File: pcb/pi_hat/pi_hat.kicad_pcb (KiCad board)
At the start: 2 copper layers, 65 x 56 mm, 3 parts, among them J1 Conn_02x20_Odd_Even, J2 RJ45, J3 RJ45

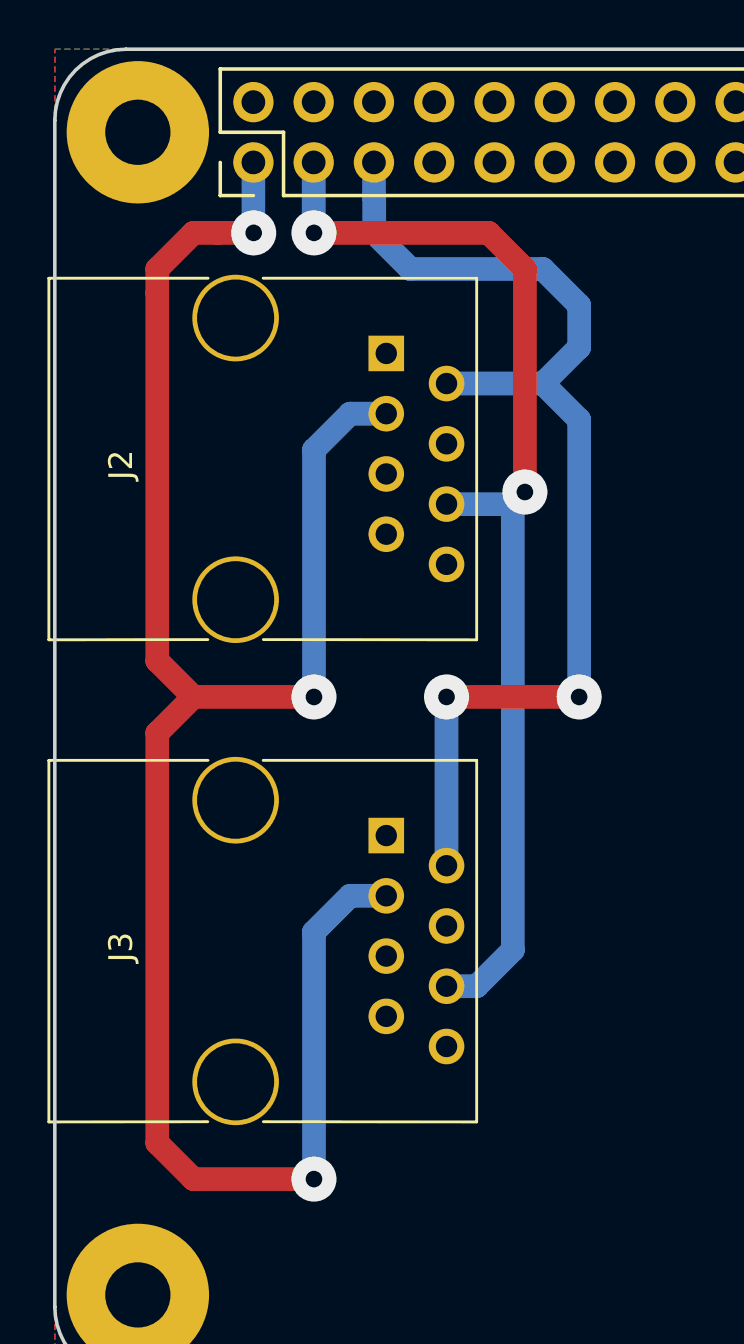
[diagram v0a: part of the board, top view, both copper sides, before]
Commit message: Trade the long ground loop for a 5th jumper :/
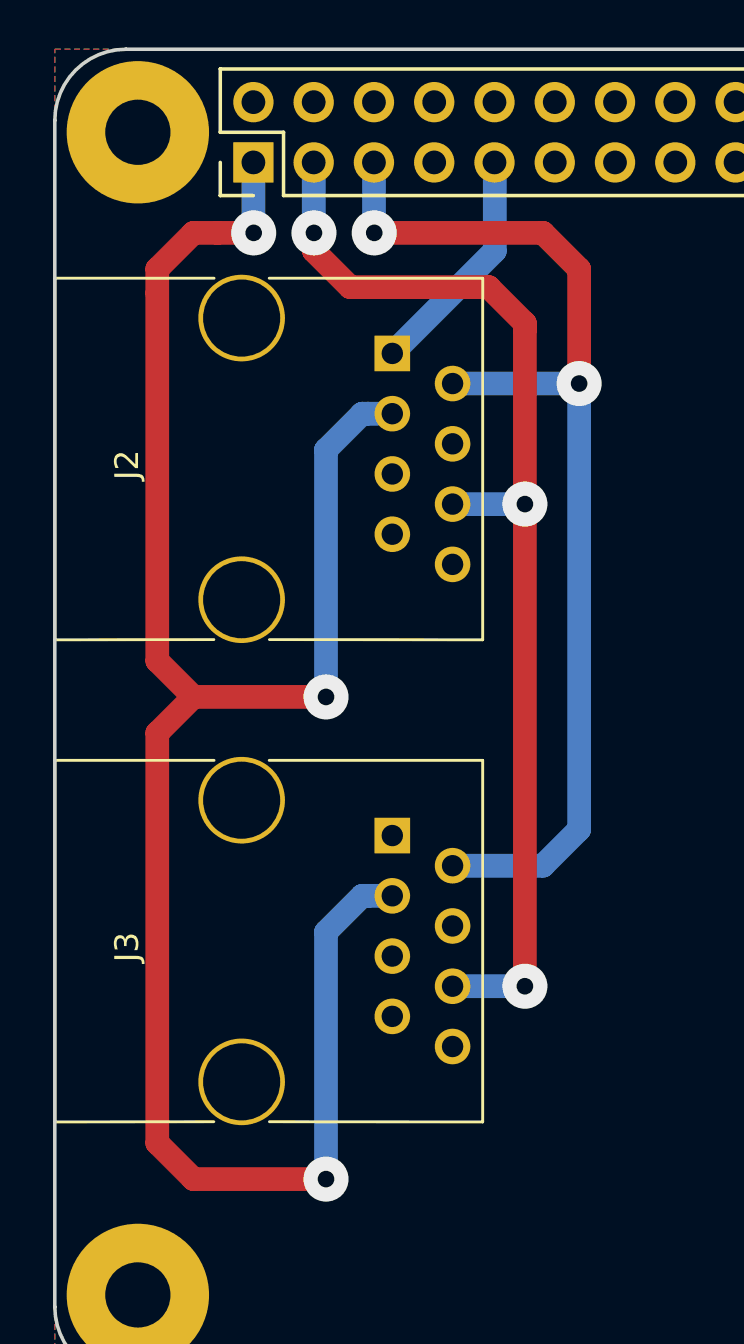
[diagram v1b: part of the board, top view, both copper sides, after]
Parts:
- moved J2 0.25 mm to (162.8, 62.2)
- moved J3 0.25 mm to (162.8, 82.5)
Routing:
- net GND: track 0.00 -> 9.88 mm
- net VCC: track 86.8 -> 87.3 mm
- net /SDA: track 47.6 -> 47.9 mm, vias 2 -> 3

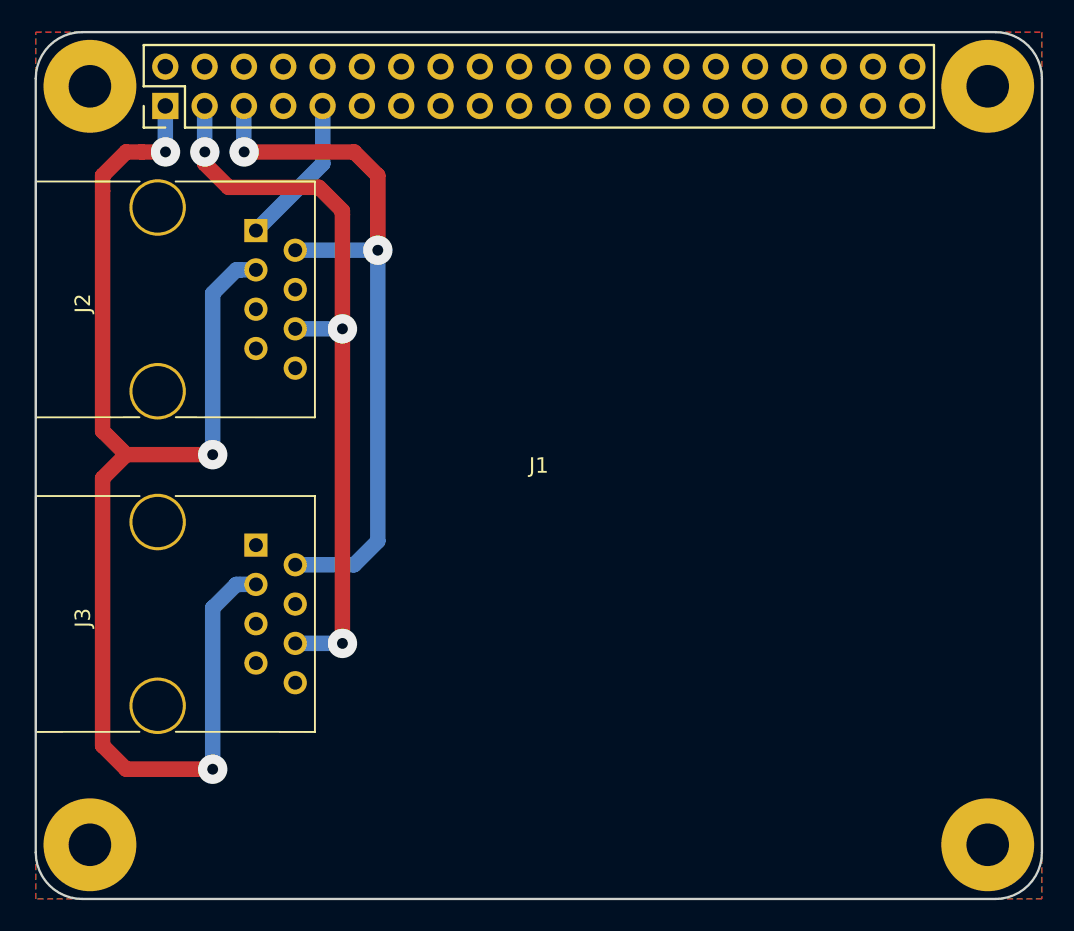
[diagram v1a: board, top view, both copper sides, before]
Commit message: Add new design with fewer jumpers and the RJ45 connectors on a side
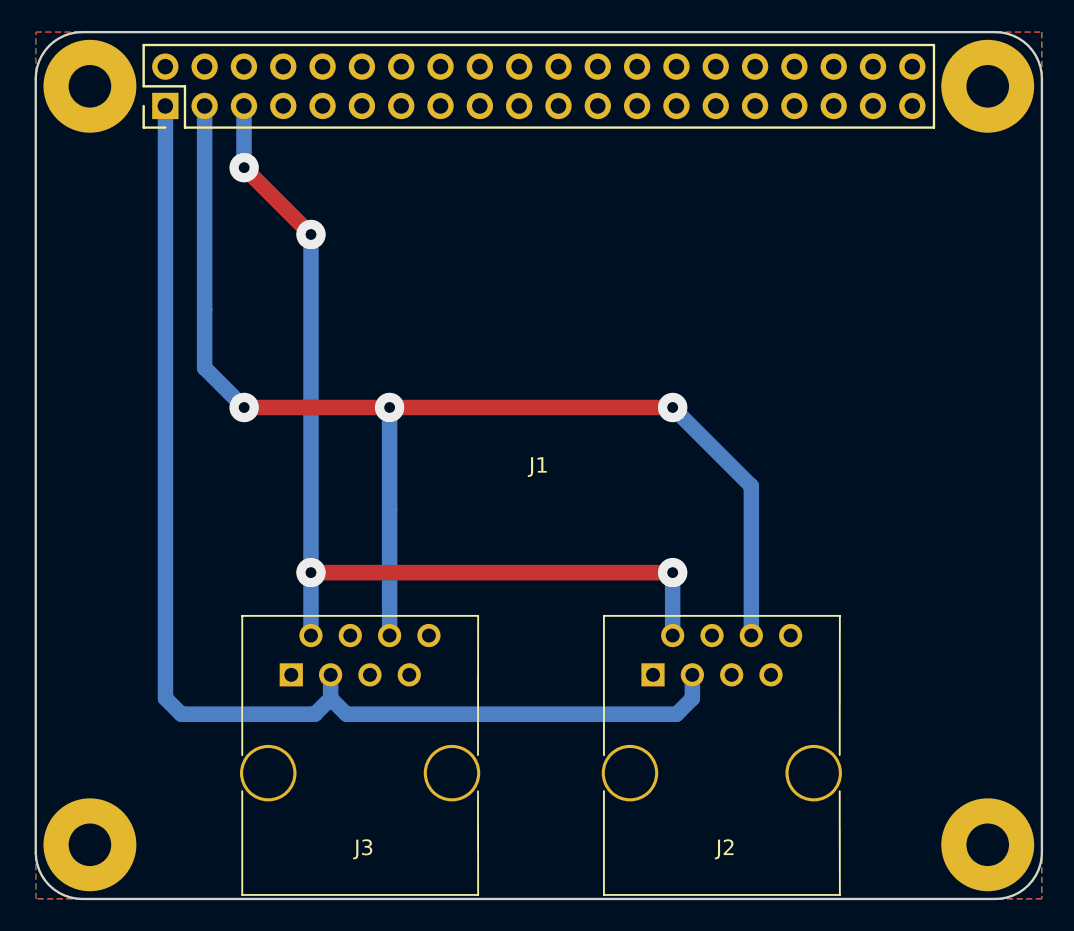
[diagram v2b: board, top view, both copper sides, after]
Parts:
- moved J2 38.5 mm to (188.5, 90.9), turned to 0 degrees
- moved J3 8.69 mm to (165.1, 90.9), turned to 0 degrees
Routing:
- net /SDA: track 47.9 -> 79.8 mm
- net /SCL: track 47.2 -> 63.4 mm, vias 2 -> 4
- net VCC: track 87.3 -> 77.6 mm, vias 3 -> 0
- net GND: track 9.88 -> 0.22 mm

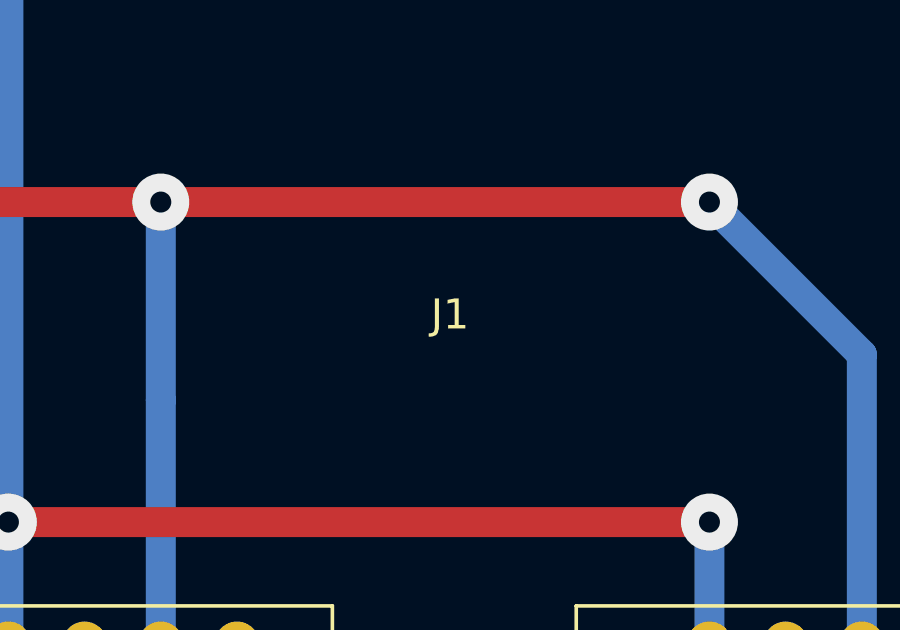
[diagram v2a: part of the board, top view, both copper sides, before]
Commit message: Add signature and version marker to the Pi hat
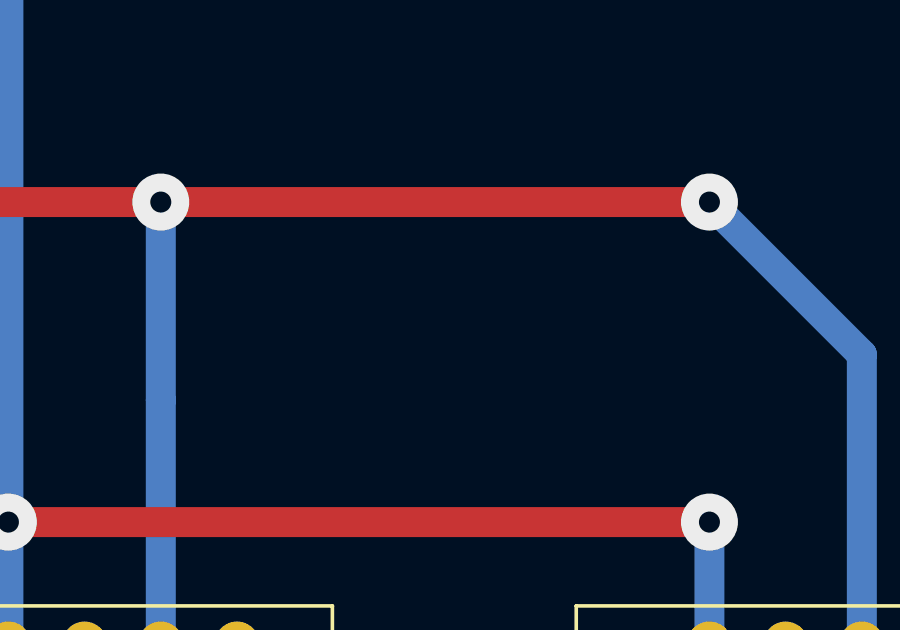
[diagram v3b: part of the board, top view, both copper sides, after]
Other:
- board text added: "Raspberry Pi RJ45 Hat Orhan 'aib' Kavrakoglu 2017-11-10"
- board text added: "v1.01 20171111"
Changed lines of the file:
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@@
     (area 148.514999 49.334999 213.665001 105.485001)
     (thickness 1.6)
-    (drawings 10)
+    (drawings 12)
     (tracks 40)
     (zones 0)
@@
   (module RaspberryPi:RaspberryPi_3_ModelB (layer F.Cu)
     (at 148.59 105.41)
-    (fp_text reference J1 (at 32.5 -28) (layer F.SilkS)
+    (fp_text reference J1 (at 32.5 -28) (layer F.SilkS) hide
       (effects (font (size 1 1) (thickness 0.15)))
     )
@@
     )
   )
+  (gr_text "v1.01 20171111" (at 165.735 101.6) (layer B.SilkS)
+    (effects (font (size 1.4 1.4) (thickness 0.3)) (justify mirror))
+  )
+  (gr_text "Raspberry Pi RJ45 Hat\nOrhan 'aib' Kavrakoglu\n2017-11-10" (at 195.58 62.23) (layer B.SilkS)
+    (effects (font (size 1.6 1.6) (thickness 0.3)) (justify mirror))
+  )
   (dimension 65 (width 0.3) (layer Margin)
